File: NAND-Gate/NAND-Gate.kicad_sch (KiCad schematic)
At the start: 8 parts, among them Q3 NPN, Q4 NPN

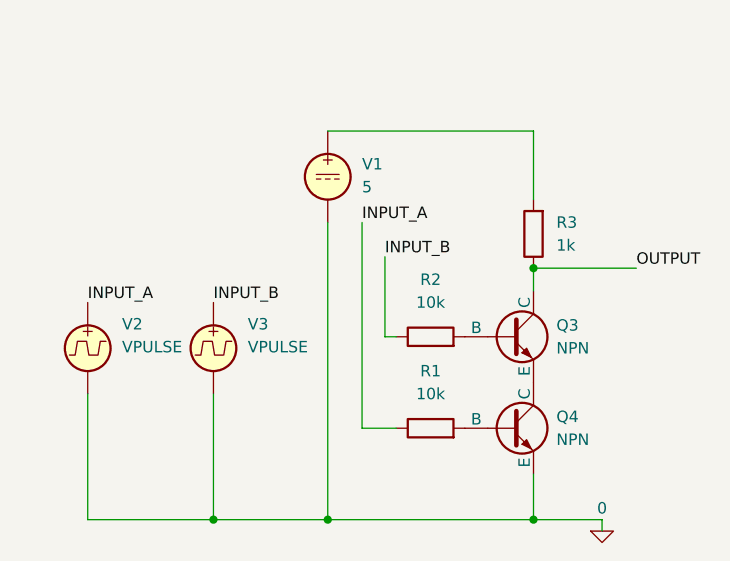
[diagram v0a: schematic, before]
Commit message: Initial commit: Add clean RTL NAND Gate schematic and simulation
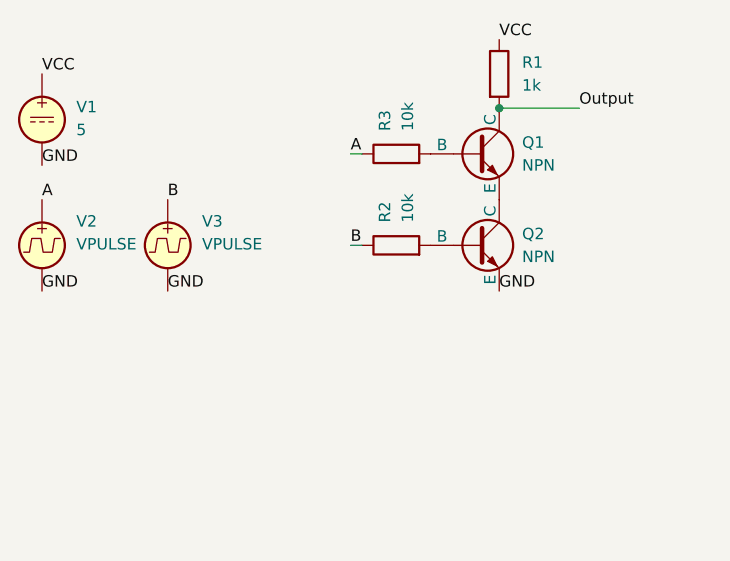
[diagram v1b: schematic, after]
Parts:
- removed Q3, Q4: NPN, symbol Simulation_SPICE:NPN
- added Q1, Q2: NPN, symbol Simulation_SPICE:NPN
- R1: value 10k -> 1k
- R3: value 1k -> 10k
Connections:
- net OUTPUT is gone; now on net A: R3.1
- net Output: now reaches R1.2
- net Output: now also Q1.1 (C)
- net at R3.2: now also Q1.2 (B); no longer V1.1
- net at R2.2: now also Q2.2 (B)
- net 0 renamed GND
- net GND: now also Q2.3 (E)
- net INPUT_A renamed A
- net A: no longer R1.1
- net INPUT_B renamed B
- new net: Q1.3 (E), Q2.1 (C)
- new net VCC: R1.1, V1.1
